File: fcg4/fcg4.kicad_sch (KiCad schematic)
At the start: 0 parts

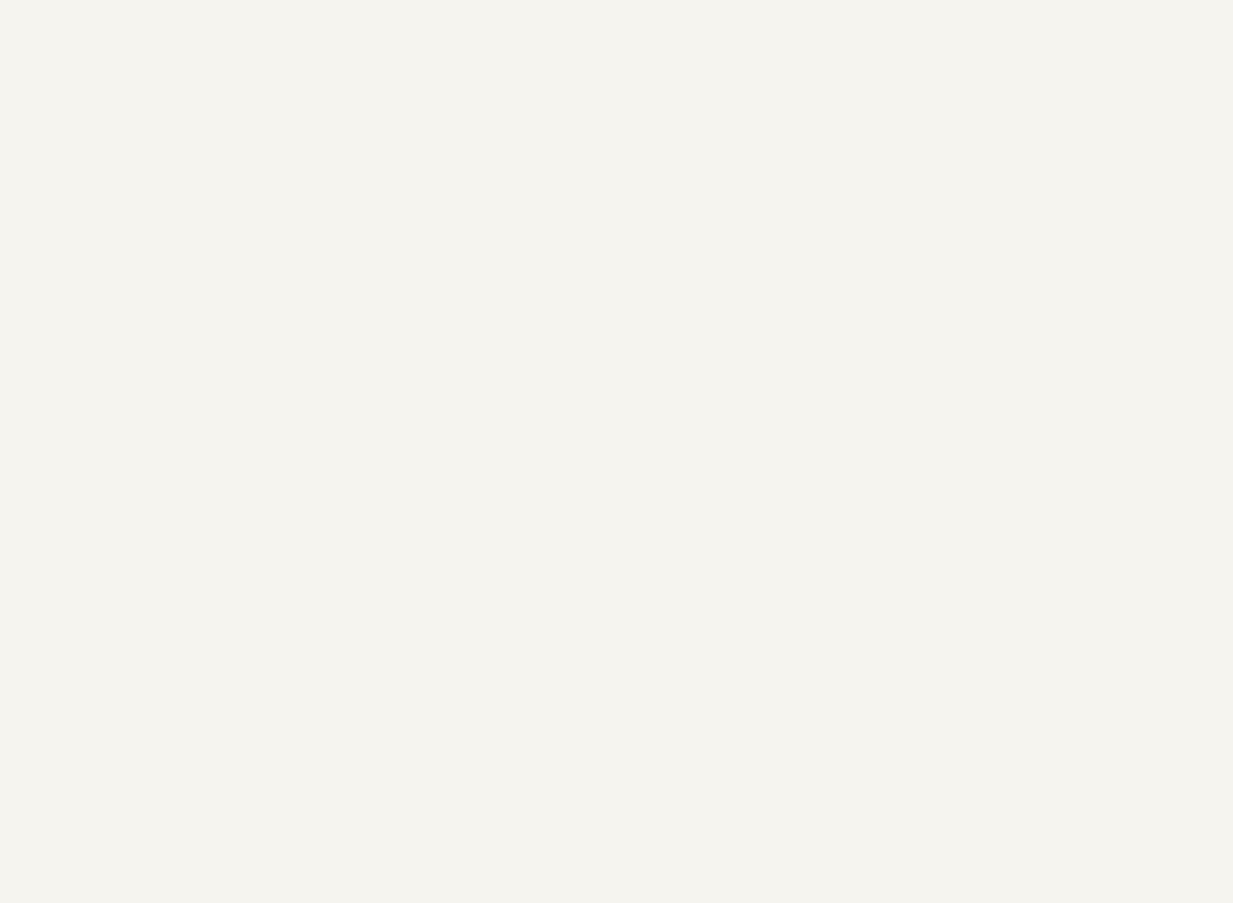
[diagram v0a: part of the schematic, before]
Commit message: add first few components
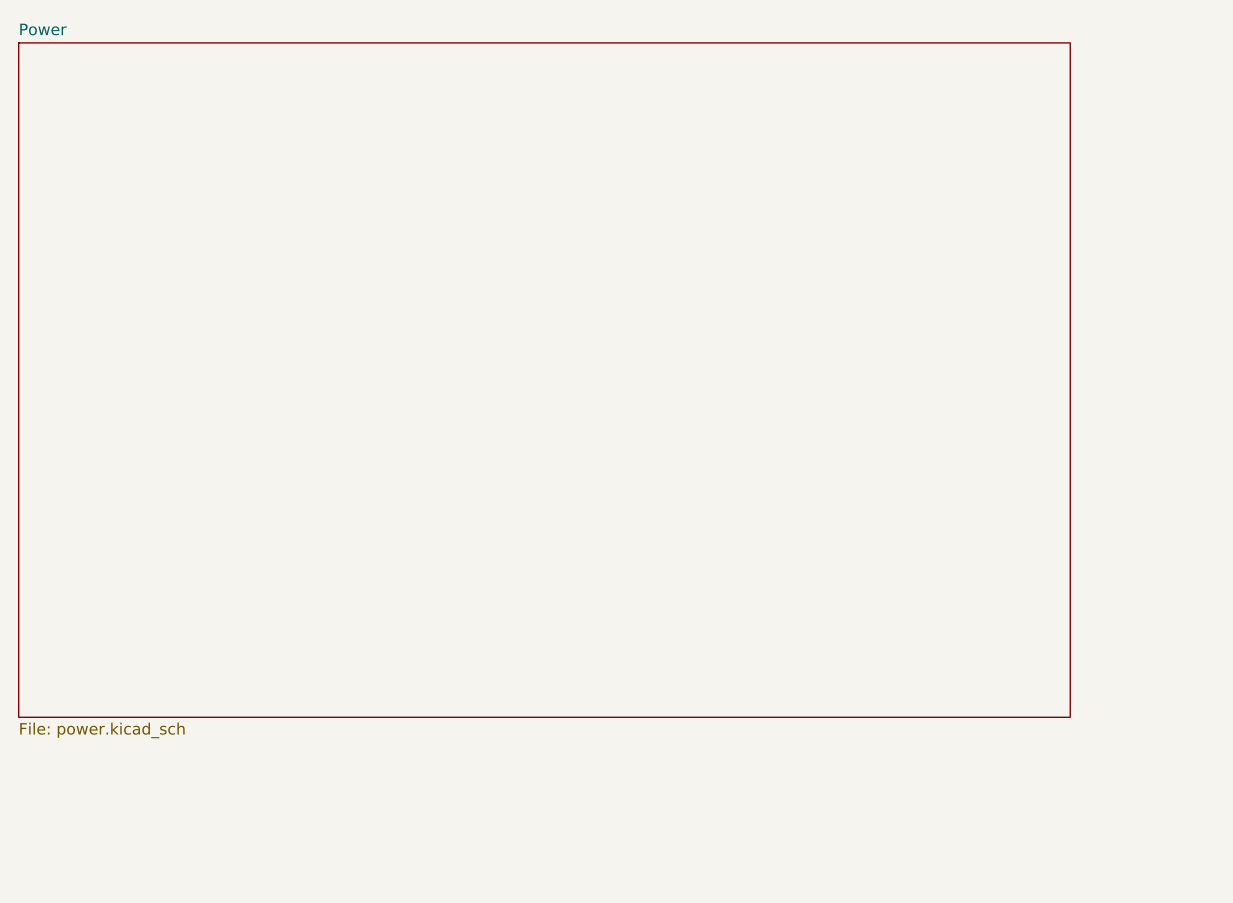
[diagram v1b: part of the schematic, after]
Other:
- added sheet Power (power.kicad_sch)
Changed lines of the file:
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@@
 	(paper "A4")
+	(sheet
+		(at -182.88 7.62)
+		(size 116.84 74.93)
+		(exclude_from_sim no)
+		(in_bom yes)
+		(on_board yes)
+		(dnp no)
+		(fields_autoplaced yes)
+		(stroke
+			(width 0.1524)
+			(type solid)
+		)
+		(fill
+			(color 0 0 0 0.0000)
+		)
+		(property "Sheetname" "Power"
+			(at -182.88 6.9084 0)
+			(effects
+				(font
+					(size 1.27 1.27)
+				)
+				(justify left bottom)
+			)
+		)
+		(property "Sheetfile" "power.kicad_sch"
+			(at -182.88 83.1346 0)
+			(effects
+				(font
+					(size 1.27 1.27)
+				)
+				(justify left top)
+			)
+		)
+		(property "Field2" ""
+			(at -182.88 7.62 0)
+			(effects
+				(font
+					(size 1.27 1.27)
+				)
+			)
+		)
+		(instances
+			(project "fcg4"
+				(path "/ebe93c2f-0aae-4f69-99fc-930f63b0ac94"
+					(page "4")
+				)
+			)
+		)
+	)
 	(sheet
 		(at 382.27 139.7)
